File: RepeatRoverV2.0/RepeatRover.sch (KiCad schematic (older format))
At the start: 5 parts

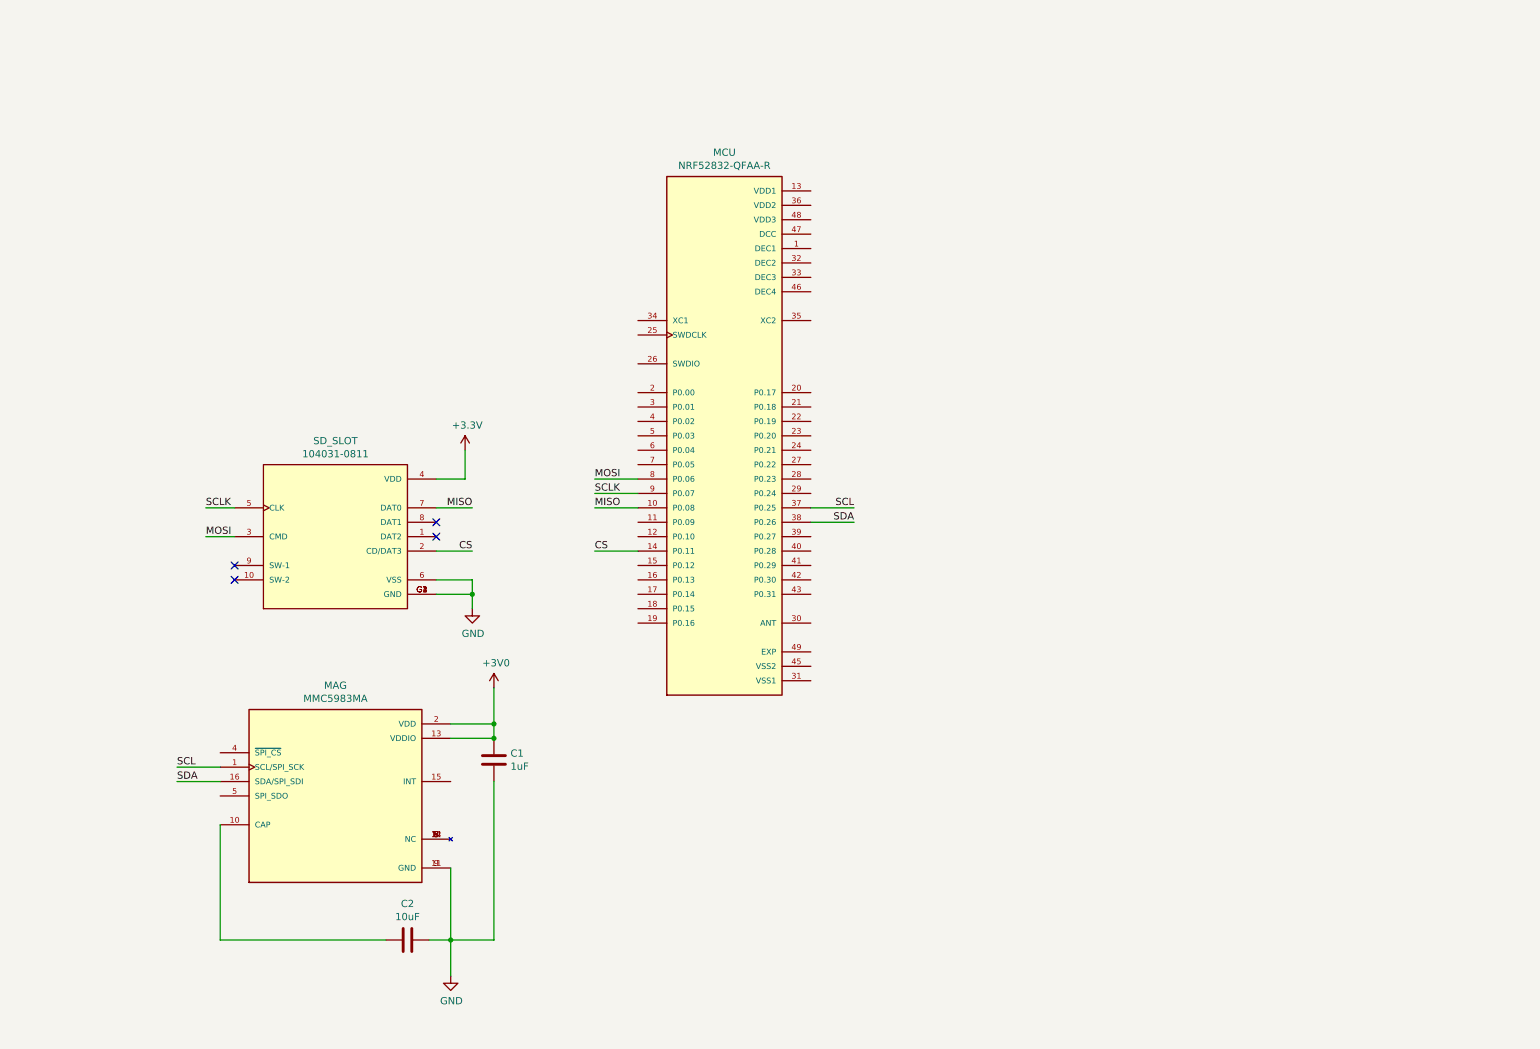
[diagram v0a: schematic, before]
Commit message: V3 W/ Partial PCB Design
Added new H-Bridge Symbol, Mapped NRF required components, finished breakout board for MMC
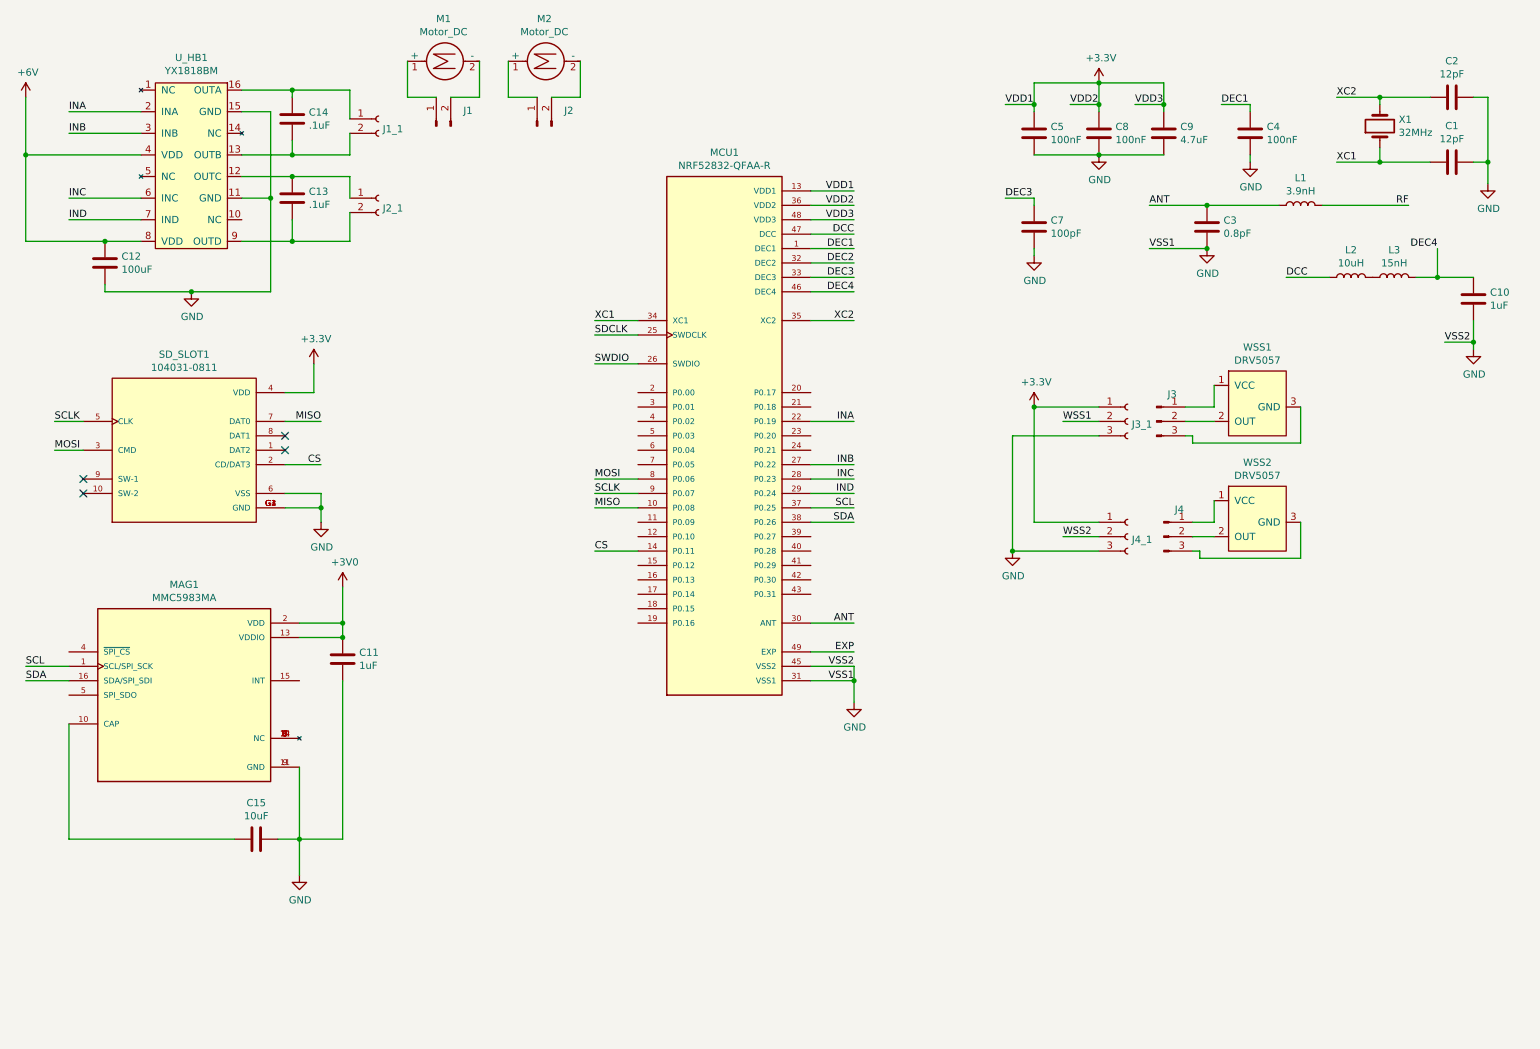
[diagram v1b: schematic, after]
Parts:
- added C1, C2: 12pF, Capacitor_SMD:C_0805_2012Metric_Pad1.18x1.45mm_HandSolder, symbol Device:C
- added C10: 1uF, Capacitor_SMD:C_0805_2012Metric_Pad1.18x1.45mm_HandSolder, symbol Device:C
- added C12: 100uF, Capacitor_SMD:C_0805_2012Metric_Pad1.18x1.45mm_HandSolder, symbol Device:C
- added C13, C14: .1uF, Capacitor_SMD:C_0805_2012Metric_Pad1.18x1.45mm_HandSolder, symbol Device:C
- added C3: 0.8pF, Capacitor_SMD:C_0805_2012Metric_Pad1.18x1.45mm_HandSolder, symbol Device:C
- added C4, C5, C8: 100nF, Capacitor_SMD:C_0805_2012Metric_Pad1.18x1.45mm_HandSolder, symbol Device:C
- added C7: 100pF, Capacitor_SMD:C_0805_2012Metric_Pad1.18x1.45mm_HandSolder, symbol Device:C
- added C9: 4.7uF, Capacitor_SMD:C_0805_2012Metric_Pad1.18x1.45mm_HandSolder, symbol Device:C
- added J1, J2: Conn_01x02_Male, symbol Connector:Conn_01x02_Male
- added J1_1, J2_1: Conn_01x02_Female, Connector_PinSocket_2.54mm:PinSocket_1x02_P2.54mm_Vertical, symbol Connector:Conn_01x02_Female
- added J3, J4: Conn_01x03_Male, symbol Connector:Conn_01x03_Male
- added J3_1, J4_1: Conn_01x03_Female, Connector_PinSocket_2.54mm:PinSocket_1x03_P2.54mm_Vertical, symbol Connector:Conn_01x03_Female
- added L1: 3.9nH, Inductor_SMD:L_0402_1005Metric_Pad0.77x0.64mm_HandSolder, symbol Device:L
- added L2: 10uH, Inductor_SMD:L_0201_0603Metric_Pad0.64x0.40mm_HandSolder, symbol Device:L
- added L3: 15nH, Inductor_SMD:L_0402_1005Metric_Pad0.77x0.64mm_HandSolder, symbol Device:L
- added M1, M2: Motor_DC, symbol Motor:Motor_DC
- added U_HB1: YX1818BM, Package_SO:SOP-16_4.55x10.3mm_P1.27mm, symbol HallEffect:YX1818BM
- added WSS1, WSS2: DRV5057, Hall Effect Footprint:SENSOR_DRV5055A2QLPGM, symbol HallEffect:DRV5057
- added X1: 32MHz, Hall Effect Footprint:OSC_XRCGB32M000FXH2CR0, symbol Device:Crystal
- C11: renamed from C1; footprint Capacitor_SMD:C_0805_2012Metric -> Capacitor_SMD:C_0805_2012Metric_Pad1.18x1.45mm_HandSolder
- C15: renamed from C2; footprint Capacitor_SMD:C_0805_2012Metric -> Capacitor_SMD:C_0805_2012Metric_Pad1.18x1.45mm_HandSolder
- renumbered MAG to MAG1, MCU to MCU1, SD_SLOT to SD_SLOT1
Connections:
- net +3V3: now also MCU1.13 (VDD1), MCU1.36 (VDD2), MCU1.48 (VDD3), C5.1, C8.1, C9.1, J3_1.1 (Pin_1), J4_1.1 (Pin_1)
- net GND: now also MCU1.31 (VSS1), MCU1.45 (VSS2), C1.2, C10.2, C12.1, C2.2, C3.2, C4.2, C5.2, C7.2, C8.2, C9.2, J3_1.3 (Pin_3), J4_1.3 (Pin_3), U_HB1.11 (GND), U_HB1.15 (GND)
- net DEC1: now reaches MCU1.1 (DEC1)
- net DEC1: now also C4.1
- net INA: now reaches MCU1.22 (P0.19)
- net INA: now also U_HB1.2 (INA)
- net SDCLK: now reaches MCU1.25 (SWDCLK)
- net SWDIO: now reaches MCU1.26 (SWDIO)
- net INB: now reaches MCU1.27 (P0.22)
- net INB: now also U_HB1.3 (INB)
- net INC: now reaches MCU1.28 (P0.23)
- net INC: now also U_HB1.6 (INC)
- net IND: now reaches MCU1.29 (P0.24)
- net IND: now also U_HB1.7 (IND)
- net ANT: now reaches MCU1.30 (ANT)
- net ANT: now also C3.1, L1.1
- net DEC2: now reaches MCU1.32 (DEC2)
- net DEC3: now reaches MCU1.33 (DEC3)
- net DEC3: now also C7.1
- net XC1: now reaches MCU1.34 (XC1)
- net XC1: now also C1.1, X1.1
- net XC2: now reaches MCU1.35 (XC2)
- net XC2: now also C2.1, X1.2
- net DEC4: now reaches MCU1.46 (DEC4)
- net DEC4: now also C10.1, L3.2
- net DCC: now reaches MCU1.47 (DCC)
- net DCC: now also L2.1
- net EXP: now reaches MCU1.49 (EXP)
- new net: J3.1 (Pin_1), WSS1.1 (VCC)
- new net: J3.2 (Pin_2), WSS1.2 (OUT)
- new net: J3.3 (Pin_3), WSS1.3 (GND)
- new net: J4.1 (Pin_1), WSS2.1 (VCC)
- new net: J4.2 (Pin_2), WSS2.2 (OUT)
- new net: J4.3 (Pin_3), WSS2.3 (GND)
- new net: C13.2, J2_1.1 (Pin_1), U_HB1.12 (OUTC)
- new net: C14.1, J1_1.2 (Pin_2), U_HB1.13 (OUTB)
- new net: C14.2, J1_1.1 (Pin_1), U_HB1.16 (OUTA)
- new net: C13.1, J2_1.2 (Pin_2), U_HB1.9 (OUTD)
- new net: J1.1 (Pin_1), M1.1 (+)
- new net: J1.2 (Pin_2), M1.2 (-)
- new net: J2.1 (Pin_1), M2.1 (+)
- new net: J2.2 (Pin_2), M2.2 (-)
- new net: L2.2, L3.1
- new net +6V: C12.2, U_HB1.4 (VDD), U_HB1.8 (VDD)
- new net RF: L1.2
- new net WSS1: J3_1.2 (Pin_2)
- new net WSS2: J4_1.2 (Pin_2)
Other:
- moved on the sheet: C11, C15, MAG1, SD_SLOT1

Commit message: PCB with revisions from lecture
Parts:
- added C16: 100uF, Capacitor_SMD:C_0805_2012Metric_Pad1.18x1.45mm_HandSolder, symbol Device:C
- added CVIN1, CVOUT1: 10uF, Capacitor_SMD:CP_Elec_5x5.7, symbol Device:CP1
- added C_RST1: 1uF, Capacitor_SMD:C_0805_2012Metric_Pad1.18x1.45mm_HandSolder, symbol Device:C
- added H1, H2, H3, H4: MountingHole, MountingHole:MountingHole_3.2mm_M3, symbol Mechanical:MountingHole
- added J5: Barrel_Jack, Connector_BarrelJack:BarrelJack_CUI_PJ-102AH_Horizontal, symbol Connector:Barrel_Jack
- added LDO1: NCP1117-3.3_SOT223, Package_TO_SOT_SMD:SOT-223-3_TabPin2, symbol Regulator_Linear:NCP1117-3.3_SOT223
- added R1, R2: 2.7k, Resistor_SMD:R_0805_2012Metric_Pad1.20x1.40mm_HandSolder, symbol Device:R_US
- added R_RST1: 10k, Resistor_SMD:R_0805_2012Metric_Pad1.20x1.40mm_HandSolder, symbol Device:R_US
- added SW_RST1: _, Button_Switch_THT:SW_PUSH_6mm, symbol Switch:SW_Push
- WSS1, WSS2: footprint Hall Effect Footprint:SENSOR_DRV5055A2QLPGM -> (none)
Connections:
- net +3V0 is gone; now on net +3V3: C11.2, MAG1.13 (VDDIO), MAG1.2 (VDD)
- net +3V3: now also CVOUT1.1, LDO1.2 (VO), R1.1, R2.1, R_RST1.1
- net +6V: now also C16.2, CVIN1.1, J5.1, LDO1.3 (VI)
- net CS: now also MCU1.21 (P0.18); no longer MCU1.14 (P0.11)
- net GND: now also C16.1, CVIN1.2, CVOUT1.2, C_RST1.2, J5.2, LDO1.1 (GND), SW_RST1.2
- net INA: now also MCU1.5 (P0.03); no longer MCU1.22 (P0.19)
- net INB: now also MCU1.6 (P0.04); no longer MCU1.27 (P0.22)
- net INC: now also MCU1.7 (P0.05); no longer MCU1.28 (P0.23)
- net IND: now also MCU1.8 (P0.06); no longer MCU1.29 (P0.24)
- net MISO: now also MCU1.24 (P0.21); no longer MCU1.10 (P0.08)
- net MOSI: now also MCU1.22 (P0.19); no longer MCU1.8 (P0.06)
- net SCL: now also MCU1.11 (P0.09), R1.2; no longer MCU1.37 (P0.25)
- net SCLK: now also MCU1.23 (P0.20); no longer MCU1.9 (P0.07)
- net SDA: now also MCU1.12 (P0.10), R2.2; no longer MCU1.38 (P0.26)
- net WSS1: now also MCU1.39 (P0.27)
- net WSS2: now also MCU1.40 (P0.28)
- new net MSCL: C_RST1.1, MCU1.29 (P0.24), R_RST1.2, SW_RST1.1
